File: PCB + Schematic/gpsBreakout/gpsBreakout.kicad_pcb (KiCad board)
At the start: 2 copper layers, 24.8 x 26.5 mm, 17 parts, among them J1 Header, U1 ATGM336H, U2 AT24CS32-STUM, U3 AT2659

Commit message: Finished board
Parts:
- moved BT1 15.2 mm to (154.6, 102.8)
- moved U2 7.78 mm to (156.4, 94.6)
- moved C5 7.78 mm to (156.5, 91.6)
- moved L1 1.52 mm to (149.2, 84.6), turned to 90 degrees
- moved JP1 0.90 mm to (146.8, 87.8)
- moved AE1 0.76 mm to (147.3, 81.7)
- moved C4 0.76 mm to (154.1, 86.9)
- moved L2 0.76 mm to (154.1, 88.8)
- moved AE2 0.63 mm to (153.3, 81.7)
- moved U3 0.56 mm to (152.4, 88.1)
- moved C3 0.53 mm to (150.5, 88.1)
- moved R1 0.27 mm to (148.7, 103.5)
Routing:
- net +3.3V: track 8.47 -> 57.1 mm, vias 2 -> 4
- net VBAT: track 0.00 -> 35.3 mm, vias 0 -> 2
- net SDA: track 0.00 -> 31.8 mm, vias 0 -> 1
- net SCL: track 0.00 -> 28.8 mm, vias 0 -> 1
- net RESET: track 0.00 -> 24.2 mm, vias 0 -> 1
- net PPS: track 0.00 -> 16.5 mm, vias 0 -> 3
- net VCC_RF: track 0.00 -> 9.19 mm
- net RF: track 0.00 -> 8.85 mm
- net TX: track 0.00 -> 7.94 mm, vias 0 -> 2
- net PASSIVE: track 0.00 -> 6.13 mm
- net GND: track 33.5 -> 39.1 mm, vias 0 -> 4
- net RX: track 0.00 -> 5.61 mm, vias 0 -> 1
- net ACTIVE: track 0.00 -> 5.60 mm
- net Net-(AE2-FEED): track 2.59 -> 2.06 mm
- added copper zone on B.Cu, net GND
- added copper zone on F.Cu, net GND
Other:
- board size 24.8 x 26.5 mm -> 18.7 x 27.1 mm
- board text added: "Designed by Charles Nicholson, June 2024"
- board text added: "GND"
- board text added: "JLCJLCJLCJLC"
- board text added: "JP1: 1 = passive, 3 = active"
- board text added: "Made with support of Hack Club and NEWBS"
- board text added: "PPS"
- board text added: "RST"
- board text added: "RX"
- board text added: "SCL"
- board text added: "SDA"
- board text added: "TX"
- board text added: "VCC"
- board text added: "V_BAT"
- board text added: "V_RF"

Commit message: Folding glider, plus some PCB stuff from later
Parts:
- AE1, AE2: footprint 1575AT43A0040E:ANT_1575AT_JOT-L -> footprints:ANT_1575AT_JOT-L
- BT1: footprint Battery:MS621R -> footprints:MS621R
- C2, C3, C5: footprint Capacitor_SMD:C_0603_1608Metric -> footprints:C_0603_1608Metric
- C4: footprint Capacitor_SMD:C_0402_1005Metric -> footprints:C_0402_1005Metric
- D1: footprint Diode_SMD:D_SMA -> footprints:D_SMA
- D2: footprint LED_SMD:LED_0603_1608Metric -> footprints:LED_0603_1608Metric
- J1: footprint Connector_PinHeader_2.54mm:PinHeader_1x10_P2.54mm_Vertical -> footprints:PinHeader_1x10_P2.54mm_Vertical
- JP1: footprint Jumper:SolderJumper-3_P1.3mm_Open_RoundedPad1.0x1.5mm -> footprints:SolderJumper-3_P1.3mm_Open_RoundedPad1.0x1.5mm
- L1, L2: footprint Inductor_SMD:L_0402_1005Metric -> footprints:L_0402_1005Metric
- R1: footprint Resistor_SMD:R_0402_1005Metric -> footprints:R_0402_1005Metric
- U1: footprint RF_GPS:ATGM336H -> footprints:ATGM336H
- U2: footprint Package_TO_SOT_SMD:SOT-23-5 -> footprints:SOT-23-5
- U3: footprint AT2659:DFN150X100X80-6N -> footprints:DFN150X100X80-6N
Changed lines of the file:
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@@
 	(net 16 "ACTIVE")
 	(net 17 "Net-(U3-RF_IN)")
-	(footprint "1575AT43A0040E:ANT_1575AT_JOT-L"
+	(footprint "footprints:ANT_1575AT_JOT-L"
 		(layer "F.Cu")
 		(at 147.32 81.661 90)
@@
 			)
 		)
-		(property "Footprint" "1575AT43A0040E:ANT_1575AT_JOT-L"
+		(property "Footprint" "footprints:ANT_1575AT_JOT-L"
 			(at 0 0 90)
 			(unlocked yes)
@@
 		)
 	)
-	(footprint "LED_SMD:LED_0603_1608Metric"
+	(footprint "footprints:LED_0603_1608Metric"
 		(layer "F.Cu")
 		(at 146.048 103.237)
@@
 			)
 		)
-		(property "Footprint" "LED_SMD:LED_0603_1608Metric"
+		(property "Footprint" "footprints:LED_0603_1608Metric"
 			(at 0 0 0)
 			(unlocked yes)
@@
 			(pintype "passive")
 		)
-		(model "${KICAD8_3DMODEL_DIR}/LED_SMD.3dshapes/LED_0603_1608Metric.wrl"
+		(model "${KIPRJMOD}/packages3D/LED_0603_1608Metric.wrl"
 			(offset
 				(xyz 0 0 0)
@@
 		)
 	)
-	(footprint "Capacitor_SMD:C_0603_1608Metric"
+	(footprint "footprints:C_0603_1608Metric"
 		(layer "F.Cu")
 		(at 150.495 88.138 -90)
@@
 			)
 		)
-		(property "Footprint" "Capacitor_SMD:C_0603_1608Metric"
+		(property "Footprint" "footprints:C_0603_1608Metric"
 			(at 0 0 -90)
 			(unlocked yes)
@@
 			(pintype "passive")
 		)
-		(model "${KICAD8_3DMODEL_DIR}/Capacitor_SMD.3dshapes/C_0603_1608Metric.wrl"
+		(model "${KIPRJMOD}/packages3D/C_0603_1608Metric.wrl"
 			(offset
 				(xyz 0 0 0)
@@
 		)
 	)
-	(footprint "1575AT43A0040E:ANT_1575AT_JOT-L"
+	(footprint "footprints:ANT_1575AT_JOT-L"
 		(layer "F.Cu")
 		(at 153.289 81.661 90)
@@
 			)
 		)
-		(property "Footprint" "1575AT43A0040E:ANT_1575AT_JOT-L"
+		(property "Footprint" "footprints:ANT_1575AT_JOT-L"
 			(at 0 0 90)
 			(unlocked yes)
@@
 		)
 	)
-	(footprint "Inductor_SMD:L_0402_1005Metric"
+	(footprint "footprints:L_0402_1005Metric"
 		(layer "F.Cu")
 		(at 149.225 84.582 90)
@@
 		(tags "inductor")
 		(property "Reference" "L1"
-			(at 1.651 0 270)
+			(at 1.651 0 -90)
 			(layer "F.SilkS")
 			(effects
@@
 			)
 		)
-		(property "Footprint" "Inductor_SMD:L_0402_1005Metric"
+		(property "Footprint" "footprints:L_0402_1005Metric"
 			(at 0 0 90)
 			(unlocked yes)
@@
 			(pintype "passive")
 		)
-		(model "${KICAD8_3DMODEL_DIR}/Inductor_SMD.3dshapes/L_0402_1005Metric.wrl"
+		(model "${KIPRJMOD}/packages3D/L_0402_1005Metric.wrl"
 			(offset
 				(xyz 0 0 0)
@@
 		)
 	)
-	(footprint "Jumper:SolderJumper-3_P1.3mm_Open_RoundedPad1.0x1.5mm"
+	(footprint "footprints:SolderJumper-3_P1.3mm_Open_RoundedPad1.0x1.5mm"
 		(layer "F.Cu")
 		(at 146.812 87.757)
@@
 			)
 		)
-		(property "Footprint" "Jumper:SolderJumper-3_P1.3mm_Open_RoundedPad1.0x1.5mm"
+		(property "Footprint" "footprints:SolderJumper-3_P1.3mm_Open_RoundedPad1.0x1.5mm"
 			(at 0 0 0)
 			(unlocked yes)
@@
 		)
 	)
-	(footprint "RF_GPS:ATGM336H"
+	(footprint "footprints:ATGM336H"
 		(layer "F.Cu")
 		(at 149.098 96.063 90)
@@
 			)
 		)
-		(property "Footprint" "RF_GPS:ATGM336H"
+		(property "Footprint" "footprints:ATGM336H"
 			(at 0 0 90)
 			(unlocked yes)
@@
 			(roundrect_rratio 0.25)
 		)
-		(model "${KICAD8_3DMODEL_DIR}/RF_GPS.3dshapes/ublox_MAX.wrl"
+		(model "${KIPRJMOD}/packages3D/ublox_MAX.wrl"
 			(offset
 				(xyz 0 0 0)
@@
 		)
 	)
-	(footprint "Capacitor_SMD:C_0603_1608Metric"
+	(footprint "footprints:C_0603_1608Metric"
 		(layer "F.Cu")
 		(at 156.464 91.578 180)
@@
 			)
 		)
-		(property "Footprint" "Capacitor_SMD:C_0603_1608Metric"
+		(property "Footprint" "footprints:C_0603_1608Metric"
 			(at 0 0 180)
 			(unlocked yes)
@@
 			(pintype "passive")
 		)
-		(model "${KICAD8_3DMODEL_DIR}/Capacitor_SMD.3dshapes/C_0603_1608Metric.wrl"
+		(model "${KIPRJMOD}/packages3D/C_0603_1608Metric.wrl"
 			(offset
 				(xyz 0 0 0)
@@
 		)
 	)
-	(footprint "Capacitor_SMD:C_0402_1005Metric"
+	(footprint "footprints:C_0402_1005Metric"
 		(layer "F.Cu")
 		(at 154.051 86.868 -90)
@@
 			)
 		)
-		(property "Footprint" "Capacitor_SMD:C_0402_1005Metric"
+		(property "Footprint" "footprints:C_0402_1005Metric"
 			(at 0 0 -90)
 			(unlocked yes)
@@
 			(pintype "passive")
 		)
-		(model "${KICAD8_3DMODEL_DIR}/Capacitor_SMD.3dshapes/C_0402_1005Metric.wrl"
+		(model "${KIPRJMOD}/packages3D/C_0402_1005Metric.wrl"
 			(offset
 				(xyz 0 0 0)
@@
 		)
 	)
-	(footprint "Inductor_SMD:L_0402_1005Metric"
+	(footprint "footprints:L_0402_1005Metric"
 		(layer "F.Cu")
 		(at 154.051 88.773 -90)
@@
 			)
 		)
-		(property "Footprint" "Inductor_SMD:L_0402_1005Metric"
+		(property "Footprint" "footprints:L_0402_1005Metric"
 			(at 0 0 -90)
 			(unlocked yes)
@@
 			(pintype "passive")
 		)
-		(model "${KICAD8_3DMODEL_DIR}/Inductor_SMD.3dshapes/L_0402_1005Metric.wrl"
+		(model "${KIPRJMOD}/packages3D/L_0402_1005Metric.wrl"
 			(offset
 				(xyz 0 0 0)
@@
 		)
 	)
-	(footprint "Diode_SMD:D_SMA"
+	(footprint "footprints:D_SMA"
 		(layer "F.Cu")
 		(at 156.337 100.33 90)
@@
 			)
 		)
-		(property "Footprint" "Diode_SMD:D_SMA"
+		(property "Footprint" "footprints:D_SMA"
 			(at 0 0 90)
 			(unlocked yes)
@@
 			(pintype "passive")
 		)
-		(model "${KICAD8_3DMODEL_DIR}/Diode_SMD.3dshapes/D_SMA.wrl"
+		(model "${KIPRJMOD}/packages3D/D_SMA.wrl"
 			(offset
 				(xyz 0 0 0)
@@
 		)
 	)
-	(footprint "Capacitor_SMD:C_0603_1608Metric"
+	(footprint "footprints:C_0603_1608Metric"
 		(layer "F.Cu")
 		(at 151.638 102.983)
@@
 			)
 		)
-		(property "Footprint" "Capacitor_SMD:C_0603_1608Metric"
+		(property "Footprint" "footprints:C_0603_1608Metric"
 			(at 0 0 0)
 			(unlocked yes)
@@
 			(pintype "passive")
 		)
-		(model "${KICAD8_3DMODEL_DIR}/Capacitor_SMD.3dshapes/C_0603_1608Metric.wrl"
+		(model "${KIPRJMOD}/packages3D/C_0603_1608Metric.wrl"
 			(offset
 				(xyz 0 0 0)
@@
 		)
 	)
-	(footprint "Package_TO_SOT_SMD:SOT-23-5"
+	(footprint "footprints:SOT-23-5"
 		(layer "F.Cu")
 		(at 156.403 94.6205 90)
@@
 			)
 		)
-		(property "Footprint" "Package_TO_SOT_SMD:SOT-23-5"
+		(property "Footprint" "footprints:SOT-23-5"
 			(at 0 0 90)
 			(unlocked yes)
@@
 			(pintype "input")
 		)
-		(model "${KICAD8_3DMODEL_DIR}/Package_TO_SOT_SMD.3dshapes/SOT-23-5.wrl"
+		(model "${KIPRJMOD}/packages3D/SOT-23-5.wrl"
 			(offset
 				(xyz 0 0 0)
@@
 		)
 	)
-	(footprint "AT2659:DFN150X100X80-6N"
+	(footprint "footprints:DFN150X100X80-6N"
 		(layer "F.Cu")
 		(at 152.4 88.138 90)
@@
 			)
 		)
-		(property "Footprint" "AT2659:DFN150X100X80-6N"
+		(property "Footprint" "footprints:DFN150X100X80-6N"
 			(at 0 0 90)
 			(unlocked yes)
@@
 		)
 	)
-	(footprint "Resistor_SMD:R_0402_1005Metric"
+	(footprint "footprints:R_0402_1005Metric"
 		(layer "F.Cu")
 		(at 148.715 103.505)
@@
 			)
 		)
-		(property "Footprint" "Resistor_SMD:R_0402_1005Metric"
+		(property "Footprint" "footprints:R_0402_1005Metric"
 			(at 0 0 0)
 			(unlocked yes)
@@
 			(pintype "passive")
 		)
-		(model "${KICAD8_3DMODEL_DIR}/Resistor_SMD.3dshapes/R_0402_1005Metric.wrl"
+		(model "${KIPRJMOD}/packages3D/R_0402_1005Metric.wrl"
 			(offset
 				(xyz 0 0 0)
@@
 		)
 	)
-	(footprint "Connector_PinHeader_2.54mm:PinHeader_1x10_P2.54mm_Vertical"
+	(footprint "footprints:PinHeader_1x10_P2.54mm_Vertical"
 		(layer "B.Cu")
 		(at 141.986 79.502 180)
@@
 			)
 		)
-		(property "Footprint" "Connector_PinHeader_2.54mm:PinHeader_1x10_P2.54mm_Vertical"
+		(property "Footprint" "footprints:PinHeader_1x10_P2.54mm_Vertical"
 			(at 0 0 0)
 			(unlocked yes)
@@
 			(pintype "passive")
 		)
-		(model "${KICAD8_3DMODEL_DIR}/Connector_PinHeader_2.54mm.3dshapes/PinHeader_1x10_P2.54mm_Vertical.wrl"
+		(model "${KIPRJMOD}/packages3D/PinHeader_1x10_P2.54mm_Vertical.wrl"
 			(offset
 				(xyz 0 0 0)
@@
 		)
 	)
-	(footprint "Battery:MS621R"
+	(footprint "footprints:MS621R"
 		(layer "B.Cu")
 		(at 154.559 102.7615 90)
@@
 			)
 		)
-		(property "Footprint" "Battery:MS621R"
+		(property "Footprint" "footprints:MS621R"
 			(at 0 0 -90)
 			(unlocked yes)

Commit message: Finished PCB
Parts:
- removed D1: SS14, footprints:D_SMA
- added R2: 1.8 K, Resistor_SMD:R_0603_1608Metric, F.Cu at (156.4, 99.4)
- added R3: 1.8 K, Resistor_SMD:R_0603_1608Metric, F.Cu at (156.4, 97.5)
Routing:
- net +3.3V: track 57.1 -> 59.9 mm
- net VBAT: track 35.3 -> 33.3 mm, vias 2 -> 1
- net SCL: track 28.8 -> 30.4 mm
- net SDA: track 31.8 -> 32.8 mm, vias 1 -> 2

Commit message: Actually finished board, did GPS work
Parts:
- removed J1: Header, footprints:PinHeader_1x10_P2.54mm_Vertical
- removed R1: 1 K, footprints:R_0402_1005Metric
- added J2: Header, Connector_PinHeader_2.54mm:PinHeader_1x11_P2.54mm_Vertical, F.Cu at (142.0, 77.0)
- added R7: 1 K, Resistor_SMD:R_0402_1005Metric, F.Cu at (148.7, 103.3)
- D2: value RED -> YELLOW; footprint footprints:LED_0603_1608Metric -> LED_SMD:LED_0603_1608Metric
- U2: value AT24CS32-STUM -> BL24C32F-RRRC; footprint footprints:SOT-23-5 -> Package_TO_SOT_SMD:SOT-23-5
- moved C3 6.61 mm to (157.1, 88.0), turned to 90 degrees
- moved AE2 4.30 mm to (156.8, 79.2)
- moved JP1 3.91 mm to (150.7, 88.5)
- moved AE1 2.89 mm to (148.9, 79.2)
- moved U3 2.80 mm to (155.2, 88.0), turned to -90 degrees
- moved L1 1.28 mm to (149.4, 85.9), turned to 0 degrees
- moved C4 0.78 mm to (153.5, 86.3)
- moved L2 0.78 mm to (153.5, 88.2)
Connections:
- net VBAT renamed V_BAT
- U1 pad 5: +3.3V -> GPS_EN
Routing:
- net GPS_EN: track 0.00 -> 13.0 mm, vias 0 -> 2
- net RF: track 8.85 -> 0.00 mm
- net +3.3V: track 59.9 -> 51.5 mm
- net PASSIVE: track 6.13 -> 0.00 mm
- net ACTIVE: track 5.60 -> 0.00 mm
- net GND: track 39.1 -> 33.5 mm
- net V_BAT: track 33.3 -> 37.1 mm
- net SDA: track 32.8 -> 36.3 mm
- net RESET: track 24.2 -> 26.7 mm
- net PPS: track 16.5 -> 19.1 mm
- net Net-(AE2-FEED): track 2.06 -> 0.00 mm
- net VCC_RF: track 9.19 -> 11.1 mm
- net Net-(U3-RF_IN): track 1.25 -> 0.00 mm
- net Net-(C4-Pad2): track 0.94 -> 0.00 mm
- net SCL: track 30.4 -> 31.0 mm
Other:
- board size 18.7 x 27.1 mm -> 18.7 x 29.3 mm

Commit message: Work on GPS
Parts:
- moved L2 3.46 mm to (156.5, 86.4), turned to 0 degrees
- moved C4 3.15 mm to (156.5, 85.2), turned to 180 degrees
- moved C3 2.02 mm to (156.5, 89.9), turned to 0 degrees
- moved L1 1.77 mm to (147.7, 85.2), turned to 180 degrees
- moved JP1 1.62 mm to (152.3, 88.5)
- moved U3 1.28 mm to (156.5, 88.0), turned to 180 degrees
- moved AE1 0.66 mm to (148.8, 79.9)
- moved AE2 0.65 mm to (157.0, 79.9)
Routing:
- net GND: track 33.5 -> 40.5 mm, vias 4 -> 28
- net PASSIVE: track 0.00 -> 6.29 mm
- net RF: track 0.00 -> 2.85 mm
- net ACTIVE: track 0.00 -> 2.54 mm
- net +3.3V: track 51.5 -> 53.3 mm
- net Net-(U3-RF_IN): track 0.00 -> 1.16 mm
- net Net-(C4-Pad2): track 0.00 -> 1.15 mm
- net Net-(AE2-FEED): track 0.00 -> 1.14 mm
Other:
- board size 18.7 x 29.3 mm -> 19.4 x 29.3 mm

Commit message: More gps work
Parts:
- AE1, AE2: value 1575AT43A0040001E -> GPS1003; footprint footprints:ANT_1575AT_JOT-L -> RF_Antenna:GPS1003
- J2: moved to B.Cu
- moved AE1 3.71 mm to (149.3, 83.6)
- moved AE2 3.69 mm to (157.2, 83.6)
- turned J2 to 180 degrees
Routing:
- net +3.3V: track 53.3 -> 51.9 mm
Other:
- board size 19.4 x 29.3 mm -> 19.4 x 32.6 mm
- board text added: "ACTIVE"
- board text added: "ATGM336H Breakout"
- board text added: "EN"
- board text added: "PASSIVE"
- board text added: "RF"

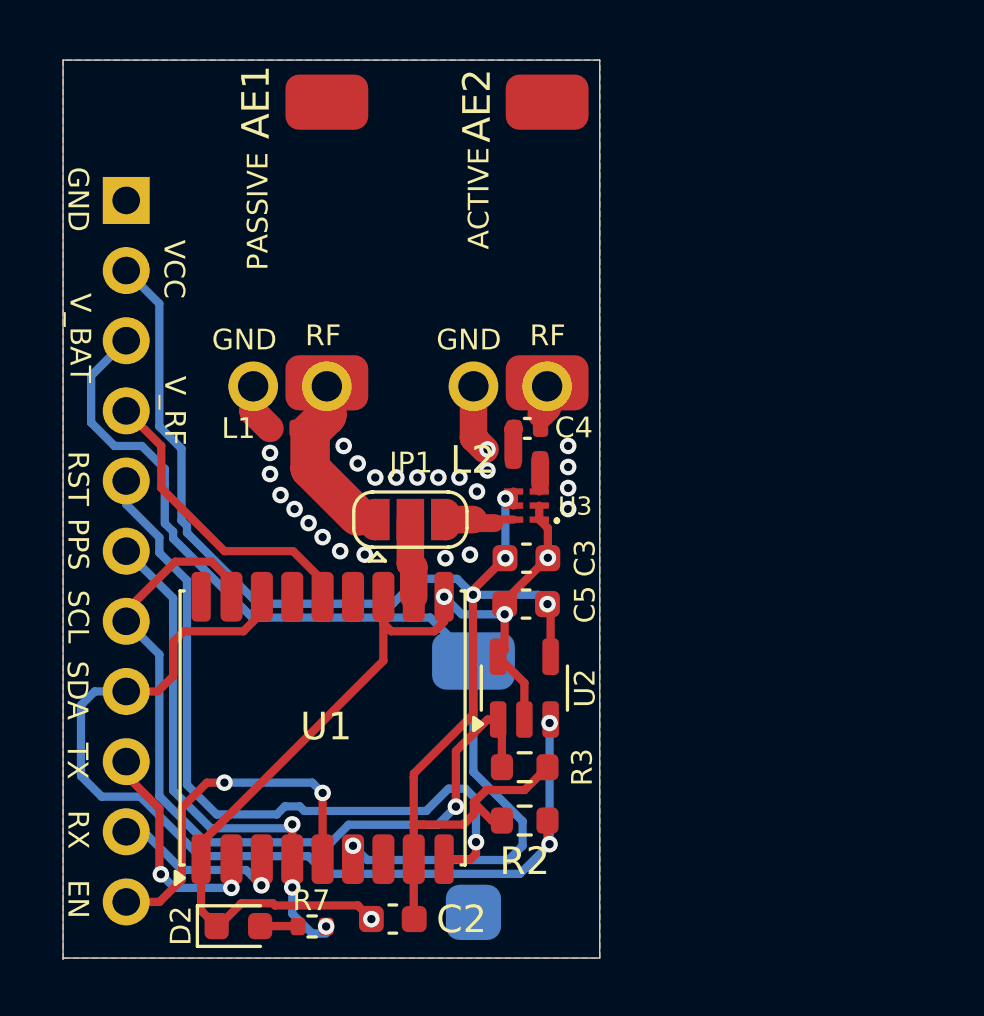
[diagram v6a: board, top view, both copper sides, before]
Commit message: GPS, IMU
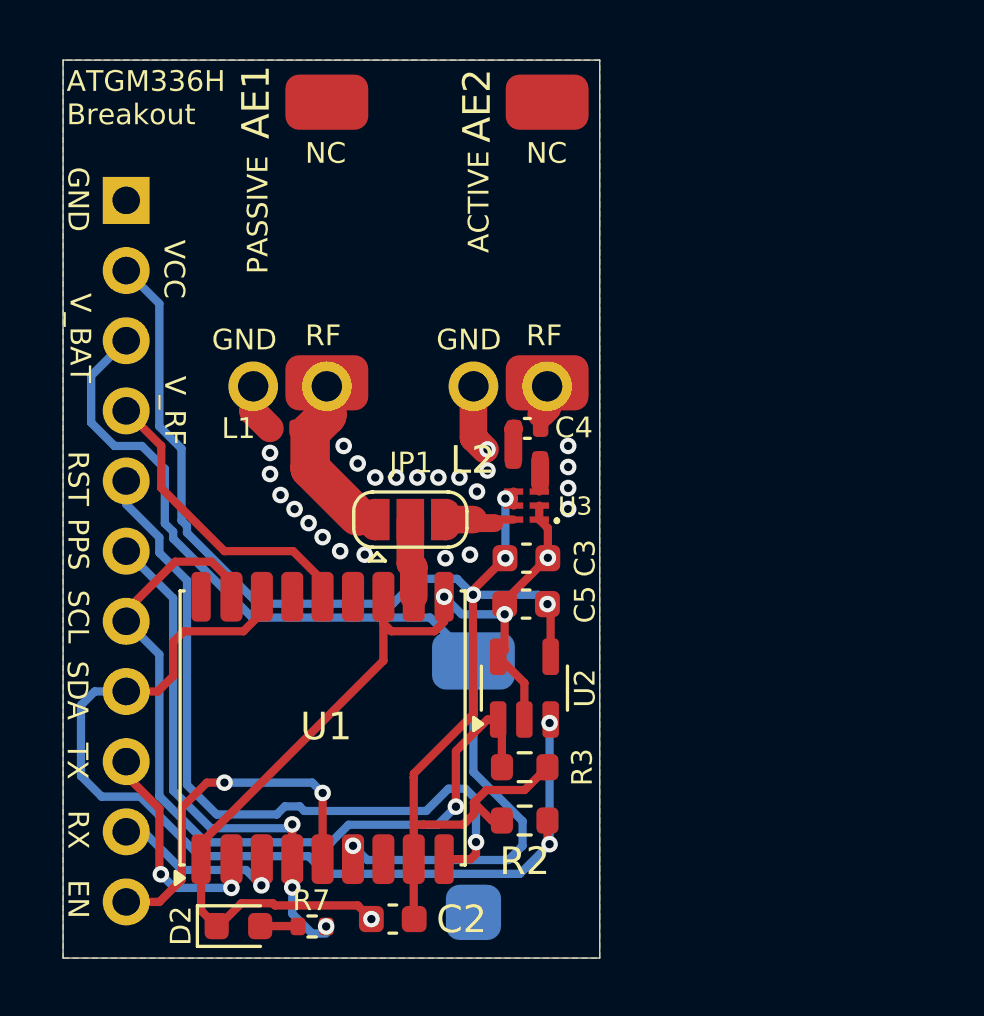
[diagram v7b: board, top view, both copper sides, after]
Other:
- board size 19.4 x 32.6 mm -> 19.4 x 32.5 mm
- board text added: "NC"
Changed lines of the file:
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@@
 		(tags "Through hole pin header THT 1x11 2.54mm single row")
 		(property "Reference" "J2"
-			(at 0 2.794 180)
+			(at 0 2.286 180)
 			(layer "B.SilkS")
 			(effects
@@
 	(gr_line
 		(start 139.7 71.882)
-		(end 139.7 104.4448)
+		(end 139.7 104.394)
 		(stroke
 			(width 0.05)
@@
 	)
 	(gr_text "Made with support \nof Hack Club and NEWBS"
-		(at 145.2372 103.886 270)
+		(at 145.923 103.886 270)
 		(layer "B.SilkS")
 		(effects
 			(font
-				(size 1 1)
-				(thickness 0.15)
+				(size 0.9 0.9)
+				(thickness 0.14)
 			)
 			(justify left bottom mirror)
@@
 	)
 	(gr_text "ATGM336H Breakout\n"
-		(at 149.7584 103.7336 270)
+		(at 149.606 103.7336 270)
 		(layer "B.SilkS")
 		(effects
@@
 	)
 	(gr_text "JP1: 1 = passive, 3 = active"
-		(at 148.5392 103.7336 270)
+		(at 158.877 73.152 0)
 		(layer "B.SilkS")
 		(effects
@@
 	)
 	(gr_text "JLCJLCJLCJLC\n"
-		(at 157.8356 83.058 270)
+		(at 159.004 74.549 0)
 		(layer "B.SilkS")
 		(effects
@@
 	)
 	(gr_text "ACTIVE\n"
-		(at 155.194 78.74 90)
+		(at 155.194 78.867 90)
 		(layer "F.SilkS")
 		(effects
@@
 		)
 	)
+	(gr_text "NC"
+		(at 156.464 75.692 0)
+		(layer "F.SilkS")
+		(effects
+			(font
+				(size 0.75 0.75)
+				(thickness 0.12)
+			)
+			(justify left bottom)
+		)
+	)
 	(gr_text "SCL"
 		(at 139.8016 91.059 -90)
@@
 	)
 	(gr_text "PASSIVE"
-		(at 147.193 79.502 90)
+		(at 147.193 79.629 90)
 		(layer "F.SilkS")
 		(effects
@@
 		)
 	)
+	(gr_text "ATGM336H\nBreakout"
+		(at 139.827 74.295 0)
+		(layer "F.SilkS")
+		(effects
+			(font
+				(size 0.75 0.75)
+				(thickness 0.12)
+			)
+			(justify left bottom)
+		)
+	)
 	(gr_text "V_RF"
 		(at 143.3068 83.312 -90)
@@
 		)
 	)
+	(gr_text "NC"
+		(at 148.463 75.692 0)
+		(layer "F.SilkS")
+		(effects
+			(font
+				(size 0.75 0.75)
+				(thickness 0.12)
+			)
+			(justify left bottom)
+		)
+	)
 	(gr_text "RF"
-		(at 156.591 82.296 0)
-		(layer "F.SilkS")
-		(effects
+		(at 156.464 82.296 0)
+		(layer "F.SilkS")
+		(effects

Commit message: Commit
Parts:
- moved R7 0.18 mm to (148.7, 103.4)
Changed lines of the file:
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@@
 		(tags "resistor")
 		(property "Reference" "R3"
-			(at -2.0828 0 270)
+			(at -2.0828 0 -90)
 			(layer "F.SilkS")
 			(effects
@@
 		)
 		(property "Value" "100 nF"
-			(at 0 1.43 360)
+			(at 0 1.43 0)
 			(layer "F.Fab")
 			(effects
@@
 		)
 		(fp_text user "${REFERENCE}"
-			(at 0 0 360)
+			(at 0 0 0)
 			(layer "F.Fab")
 			(effects
@@
 	(footprint "Resistor_SMD:R_0402_1005Metric"
 		(layer "F.Cu")
-		(at 148.717 103.251)
+		(at 148.717 103.4288)
 		(descr "Resistor SMD 0402 (1005 Metric), square (rectangular) end terminal, IPC_7351 nominal, (Body size source: IPC-SM-782 page 72, https://www.pcb-3d.com/wordpress/wp-content/uploads/ipc-sm-782a_amendment_1_and_2.pdf), generated with kicad-footprint-generator")
 		(tags "resistor")
@@
 		)
 		(pad "1" thru_hole circle
-			(at -0.127 0 90)
+			(at 0 0 90)
 			(size 1.8 1.8)
 			(drill 1.1)
@@
 		)
 		(pad "2" thru_hole circle
-			(at -0.127 -2.667 90)
+			(at 0 -2.921 90)
 			(size 1.8 1.8)
 			(drill 1.1)
@@
 		(tags "capacitor")
 		(property "Reference" "C5"
-			(at -2.1336 -0.0144 270)
+			(at -2.1336 -0.0144 -90)
 			(layer "F.SilkS")
 			(effects
@@
 		(tags "inductor")
 		(property "Reference" "L2"
-			(at -1.9534 0 360)
+			(at -1.9534 0 0)
 			(layer "F.SilkS")
 			(effects
@@
 		)
 		(property "Value" "6.8 nH"
-			(at 0 1.17 360)
+			(at 0 1.17 0)
 			(layer "F.Fab")
 			(effects
@@
 		)
 		(fp_text user "${REFERENCE}"
-			(at 0 0 360)
+			(at 0 0 0)
 			(layer "F.Fab")
 			(effects
@@
 		)
 		(pad "1" thru_hole circle
-			(at -0.127 0 90)
+			(at 0 0 90)
 			(size 1.8 1.8)
 			(drill 1.1)
@@
 		)
 		(pad "2" thru_hole circle
-			(at -0.127 -2.667 90)
+			(at 0 -2.921 90)
 			(size 1.8 1.8)
 			(drill 1.1)
@@
 	)
 	(gr_text "GND"
-		(at 145.0848 82.4484 0)
+		(at 145.0848 82.296 0)
 		(layer "F.SilkS")
 		(effects
@@
 	)
 	(gr_text "GND"
-		(at 153.2128 82.4484 0)
+		(at 153.1112 82.296 0)
 		(layer "F.SilkS")
 		(effects
@@
 	)
 	(segment
-		(start 148.207 103.251)
-		(end 148.193 103.237)
+		(start 148.1816 103.2256)
+		(end 146.8469 103.2256)
 		(width 0.3)
 		(layer "F.Cu")
@@
 	)
 	(segment
-		(start 148.193 103.237)
+		(start 146.8469 103.2256)
 		(end 146.8355 103.237)
 		(width 0.3)
@@
 		(net 6)
 	)
+	(segment
+		(start 148.207 103.251)
+		(end 148.1816 103.2256)
+		(width 0.3)
+		(layer "F.Cu")
+		(net 6)
+	)
 	(via
 		(at 146.881335 101.762)
@@
 	)
 	(via
-		(at 149.225 103.251)
+		(at 149.227 103.4288)
 		(size 0.6)
 		(drill 0.3)
@@
 		(polygon
 			(pts
-				(xy 144.526 71.882) (xy 159.131 71.882) (xy 159.131 85.471) (xy 144.526 85.471)
+				(xy 142.0368 71.882) (xy 159.131 71.882) (xy 159.131 85.471) (xy 142.0368 85.471)
 			)
 		)
